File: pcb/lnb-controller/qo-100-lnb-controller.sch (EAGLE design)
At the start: 168 parts, among them CON1 3P-SH-SIDE, CON2 2EDG-2P-5MM, U1 EFM32TG11B120F128GM32, U2 DSB321SDA, U3 SI5351C-B-GM, U4 LT8650S-1, U5 MCP4728-A2, U6 MIC23155, U7 LT8636, U8 ADP7142AUJZ-3.3

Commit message: Update I2C slave resistors to minimize load effect when powered down
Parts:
- R4, R5: value 0 Ohms -> 1K Ohms
- R45, R46: value 1K Ohms -> 47K Ohms
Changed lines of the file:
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@@
 <part name="CON1" library="JST" deviceset="3P" device="-SH-SIDE" value="3P-SH-SIDE"/>
 <part name="GND24" library="Supply Symbol" deviceset="GND" device=""/>
-<part name="R4" library="Resistor" deviceset="RESISTOR" device="-0603" value="0 Ohms"/>
-<part name="R5" library="Resistor" deviceset="RESISTOR" device="-0603" value="0 Ohms"/>
+<part name="R4" library="Resistor" deviceset="RESISTOR" device="-0603" value="1K Ohms"/>
+<part name="R5" library="Resistor" deviceset="RESISTOR" device="-0603" value="1K Ohms"/>
 <part name="C3" library="Capacitor" deviceset="CAPACITOR" device="-0603" value="100nF"/>
 <part name="GND26" library="Supply Symbol" deviceset="GND" device=""/>
@@
 <part name="C4" library="Capacitor" deviceset="CAPACITOR" device="-0603" value="1uF"/>
 <part name="U1" library="EFM32" deviceset="EFM32TG11B1*M32" device="" technology="20F128G"/>
-<part name="R45" library="Resistor" deviceset="RESISTOR" device="-0603" value="1K Ohms"/>
+<part name="R45" library="Resistor" deviceset="RESISTOR" device="-0603" value="47K Ohms"/>
 <part name="3V14" library="Supply Symbol" deviceset="3V3" device=""/>
-<part name="R46" library="Resistor" deviceset="RESISTOR" device="-0603" value="1K Ohms"/>
+<part name="R46" library="Resistor" deviceset="RESISTOR" device="-0603" value="47K Ohms"/>
 <part name="3V15" library="Supply Symbol" deviceset="3V3" device=""/>
 </parts>

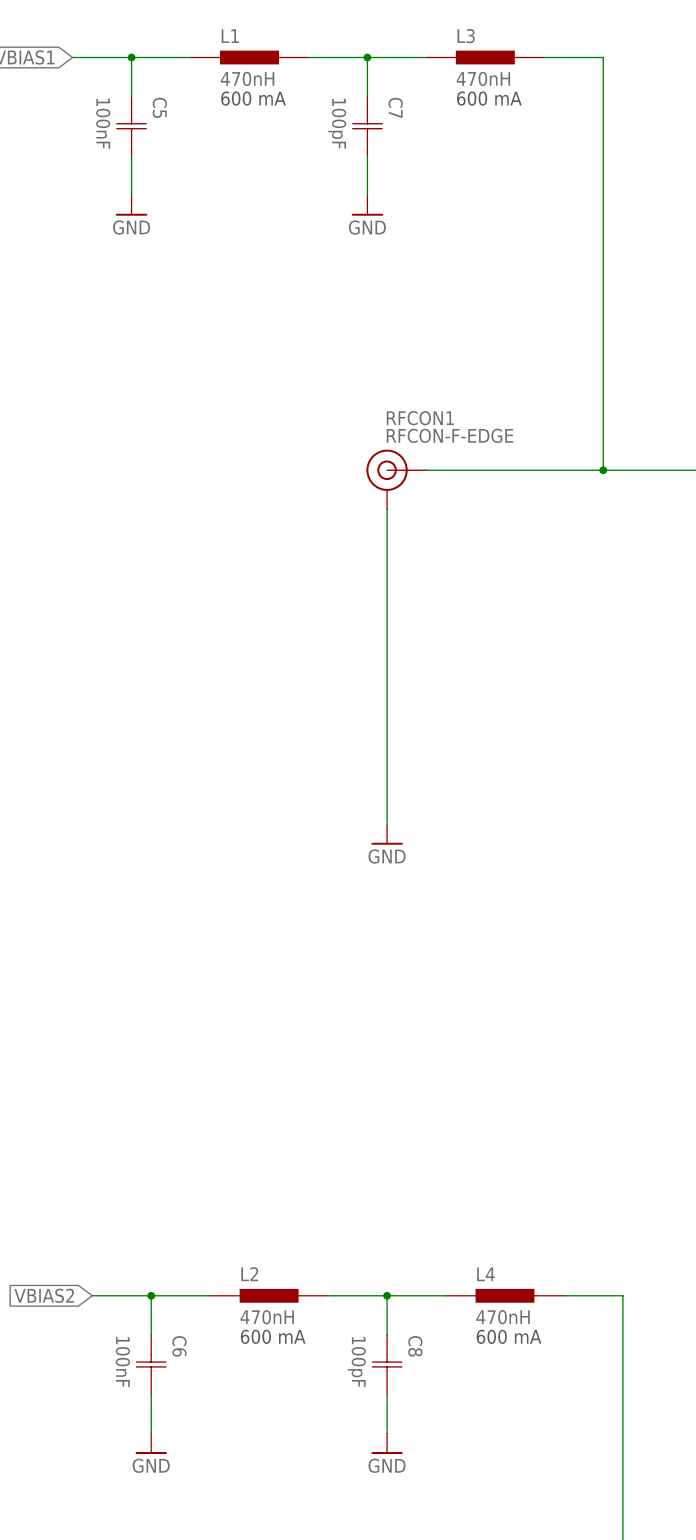
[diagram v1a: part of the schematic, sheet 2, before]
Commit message: Assembly LNB Controller changes
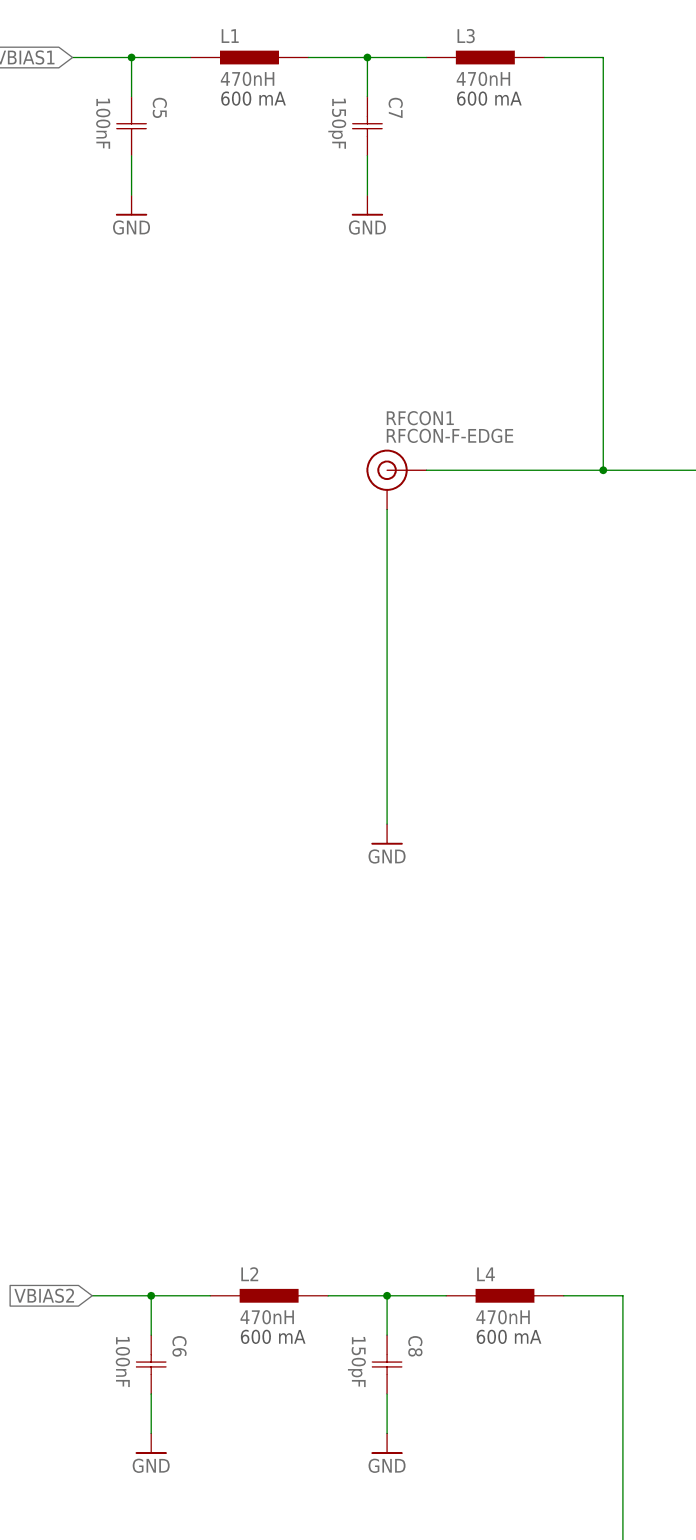
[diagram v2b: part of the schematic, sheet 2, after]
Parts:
- C7, C8: value 100pF -> 150pF
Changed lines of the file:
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@@
 <part name="C5" library="Capacitor" deviceset="CAPACITOR" device="-0603" value="100nF"/>
 <part name="GND19" library="Supply Symbol" deviceset="GND" device=""/>
-<part name="C7" library="Capacitor" deviceset="CAPACITOR" device="-0603" value="100pF"/>
+<part name="C7" library="Capacitor" deviceset="CAPACITOR" device="-0603" value="150pF"/>
 <part name="GND21" library="Supply Symbol" deviceset="GND" device=""/>
 <part name="C21" library="Capacitor" deviceset="CAPACITOR" device="-0603" value="100pF"/>
@@
 <part name="C6" library="Capacitor" deviceset="CAPACITOR" device="-0603" value="100nF"/>
 <part name="GND64" library="Supply Symbol" deviceset="GND" device=""/>
-<part name="C8" library="Capacitor" deviceset="CAPACITOR" device="-0603" value="100pF"/>
+<part name="C8" library="Capacitor" deviceset="CAPACITOR" device="-0603" value="150pF"/>
 <part name="GND66" library="Supply Symbol" deviceset="GND" device=""/>
 <part name="C22" library="Capacitor" deviceset="CAPACITOR" device="-0603" value="100pF"/>

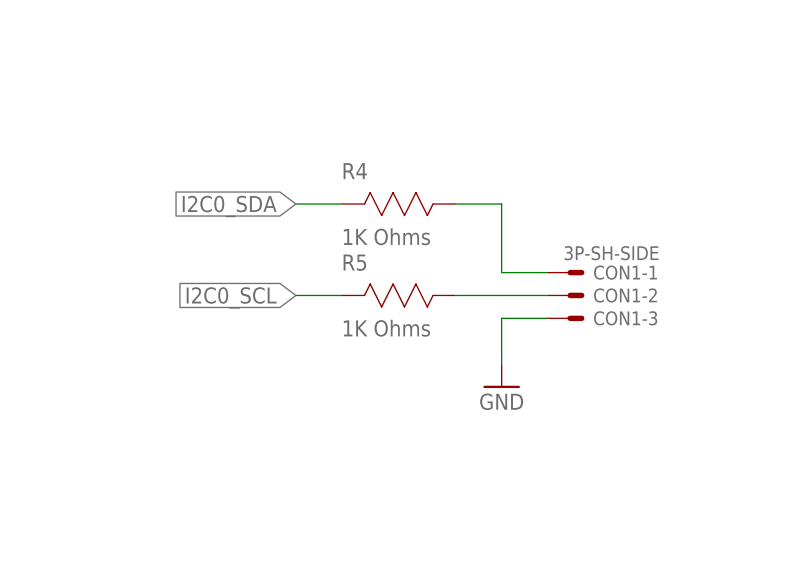
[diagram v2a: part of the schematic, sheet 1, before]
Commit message: Revert I2C resistor chnges because they do not work
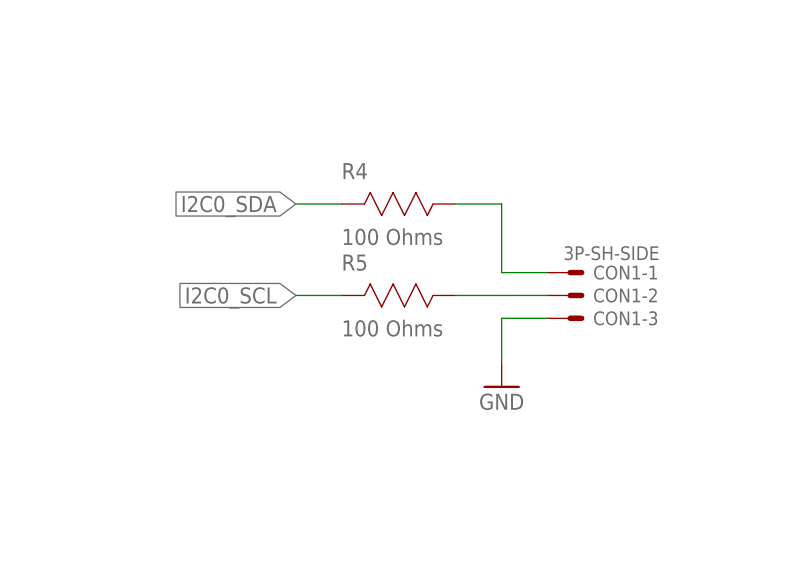
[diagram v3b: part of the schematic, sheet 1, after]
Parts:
- R4, R5: value 1K Ohms -> 100 Ohms
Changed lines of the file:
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@@
 <part name="CON1" library="JST" deviceset="3P" device="-SH-SIDE" value="3P-SH-SIDE"/>
 <part name="GND24" library="Supply Symbol" deviceset="GND" device=""/>
-<part name="R4" library="Resistor" deviceset="RESISTOR" device="-0603" value="1K Ohms"/>
-<part name="R5" library="Resistor" deviceset="RESISTOR" device="-0603" value="1K Ohms"/>
+<part name="R4" library="Resistor" deviceset="RESISTOR" device="-0603" value="100 Ohms"/>
+<part name="R5" library="Resistor" deviceset="RESISTOR" device="-0603" value="100 Ohms"/>
 <part name="C3" library="Capacitor" deviceset="CAPACITOR" device="-0603" value="100nF"/>
 <part name="GND26" library="Supply Symbol" deviceset="GND" device=""/>
